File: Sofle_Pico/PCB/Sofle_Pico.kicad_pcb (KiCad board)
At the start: 2 copper layers, 145.4 x 116.3 mm, 129 parts, among them J1 Conn_01x05, J2 4PIN, J3 Conn_01x04, J4 Conn_01x04, J5 Conn_01x05, J6 Conn_01x05, J7 Conn_01x04, Q1 DMG2305UX, SW1 SW_PUSH, SW10 SW_PUSH, SW11 SW_PUSH, SW12 SW_PUSH, SW13 SW_PUSH, SW14 SW_PUSH, SW15 SW_PUSH, SW16 SW_PUSH, SW17 SW_PUSH, SW18 SW_PUSH, SW19 SW_PUSH, SW2 SW_PUSH, SW20 SW_PUSH, SW21 SW_PUSH, SW22 SW_PUSH, SW23 SW_PUSH, SW24 SW_PUSH, SW25 Rotary_Encoder_Switch-Device, SW26 SW_PUSH, SW27 SW_PUSH, SW28 SW_PUSH, SW29 SW_PUSH, SW3 SW_PUSH, SW30 SW_PUSH, SW4 SW_PUSH, SW5 SW_PUSH, SW6 SW_PUSH, SW7 SW_PUSH, SW8 SW_PUSH, SW9 SW_PUSH, U1 SN74AHCT1G125, U2 Pico

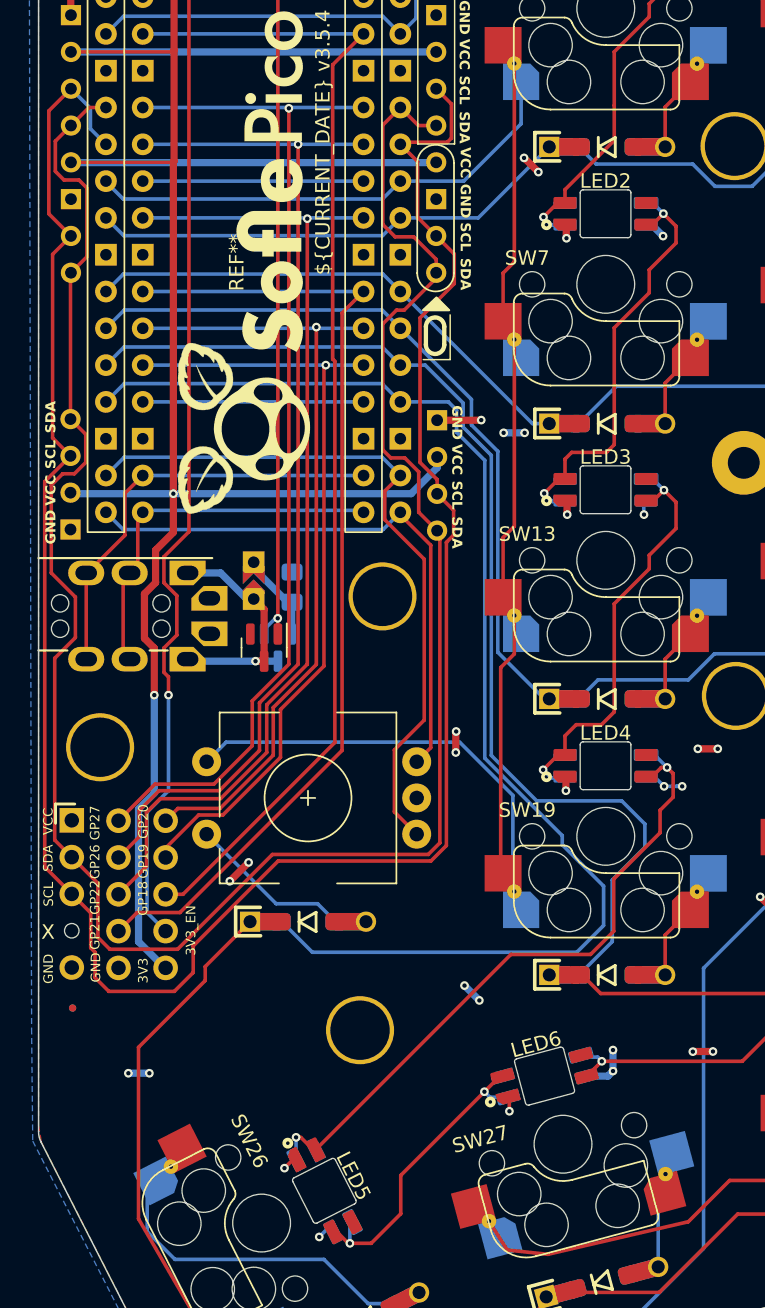
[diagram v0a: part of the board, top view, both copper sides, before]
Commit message: i2c routing / stubbing / OLED routing fixes
Fixed stitching broken by clean-up tool
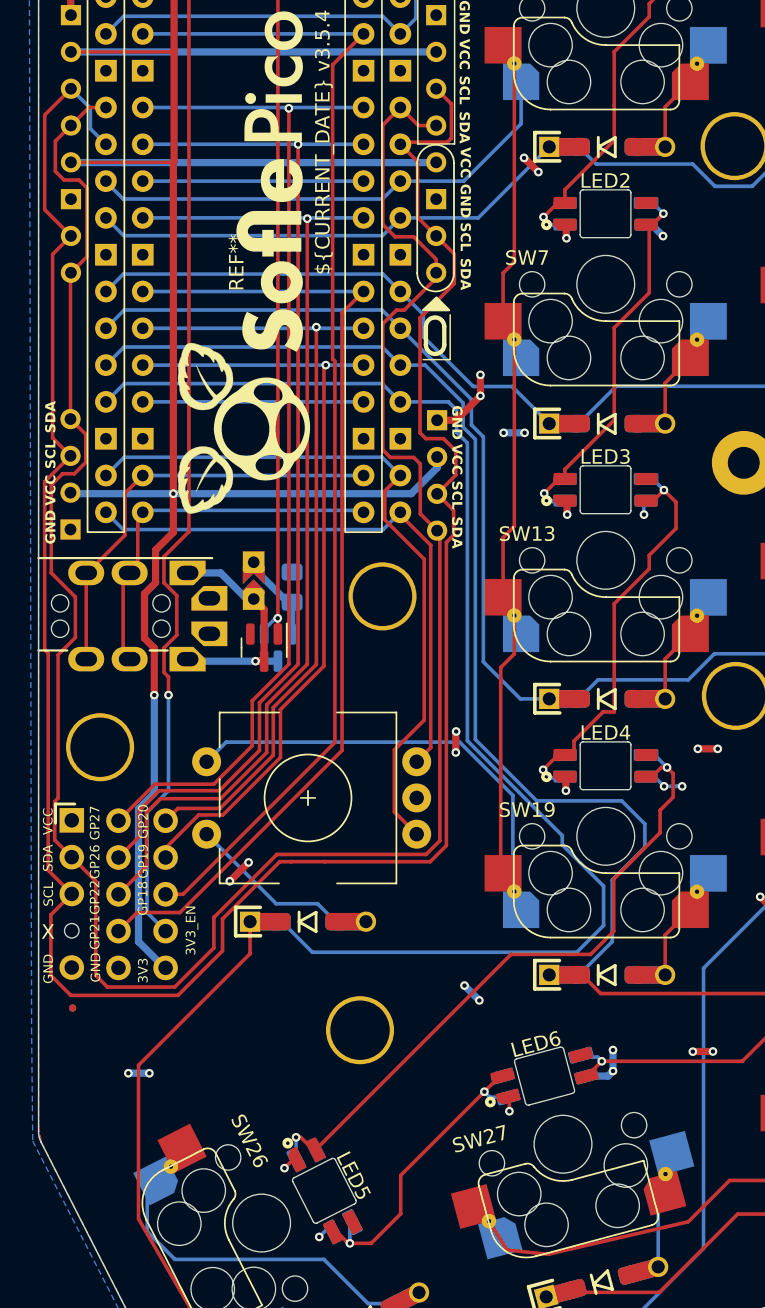
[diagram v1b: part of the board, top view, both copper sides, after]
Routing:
- net SCL: track 160.2 -> 165.5 mm
- net SDA: track 153.4 -> 158.7 mm
- net Net-(LED2-DOUT): track 30.4 -> 28.3 mm
- net GND: track 88.7 -> 90.8 mm, vias 96 -> 97
- net row2: track 146.2 -> 147.2 mm
- net row1: track 129.0 -> 129.8 mm
